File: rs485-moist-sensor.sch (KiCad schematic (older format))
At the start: 31 parts, among them IC1 ATTINY441-SSU, P1 CONN_02X03, P2 CONN_01X04, Q1 Q_PMOS_GSD, U1 SN65HVD72, U2 MCP1702, X1 16MHz

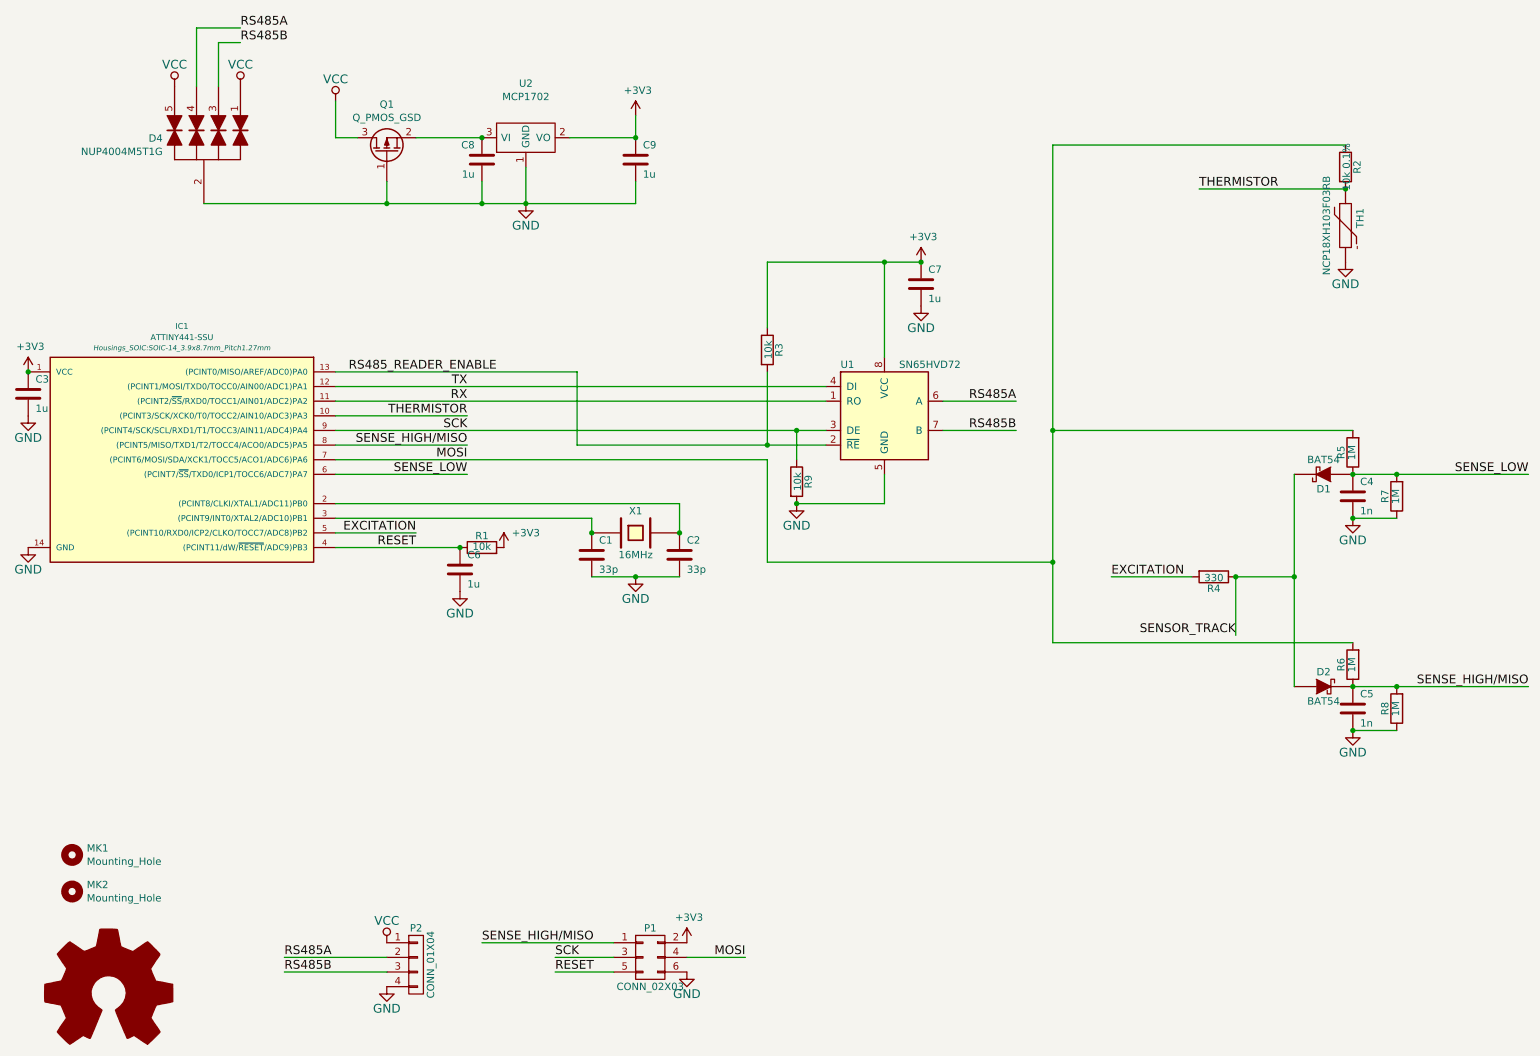
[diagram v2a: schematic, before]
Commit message: Update capacitance to accomodate crystal change. Tidyup fabrication layers
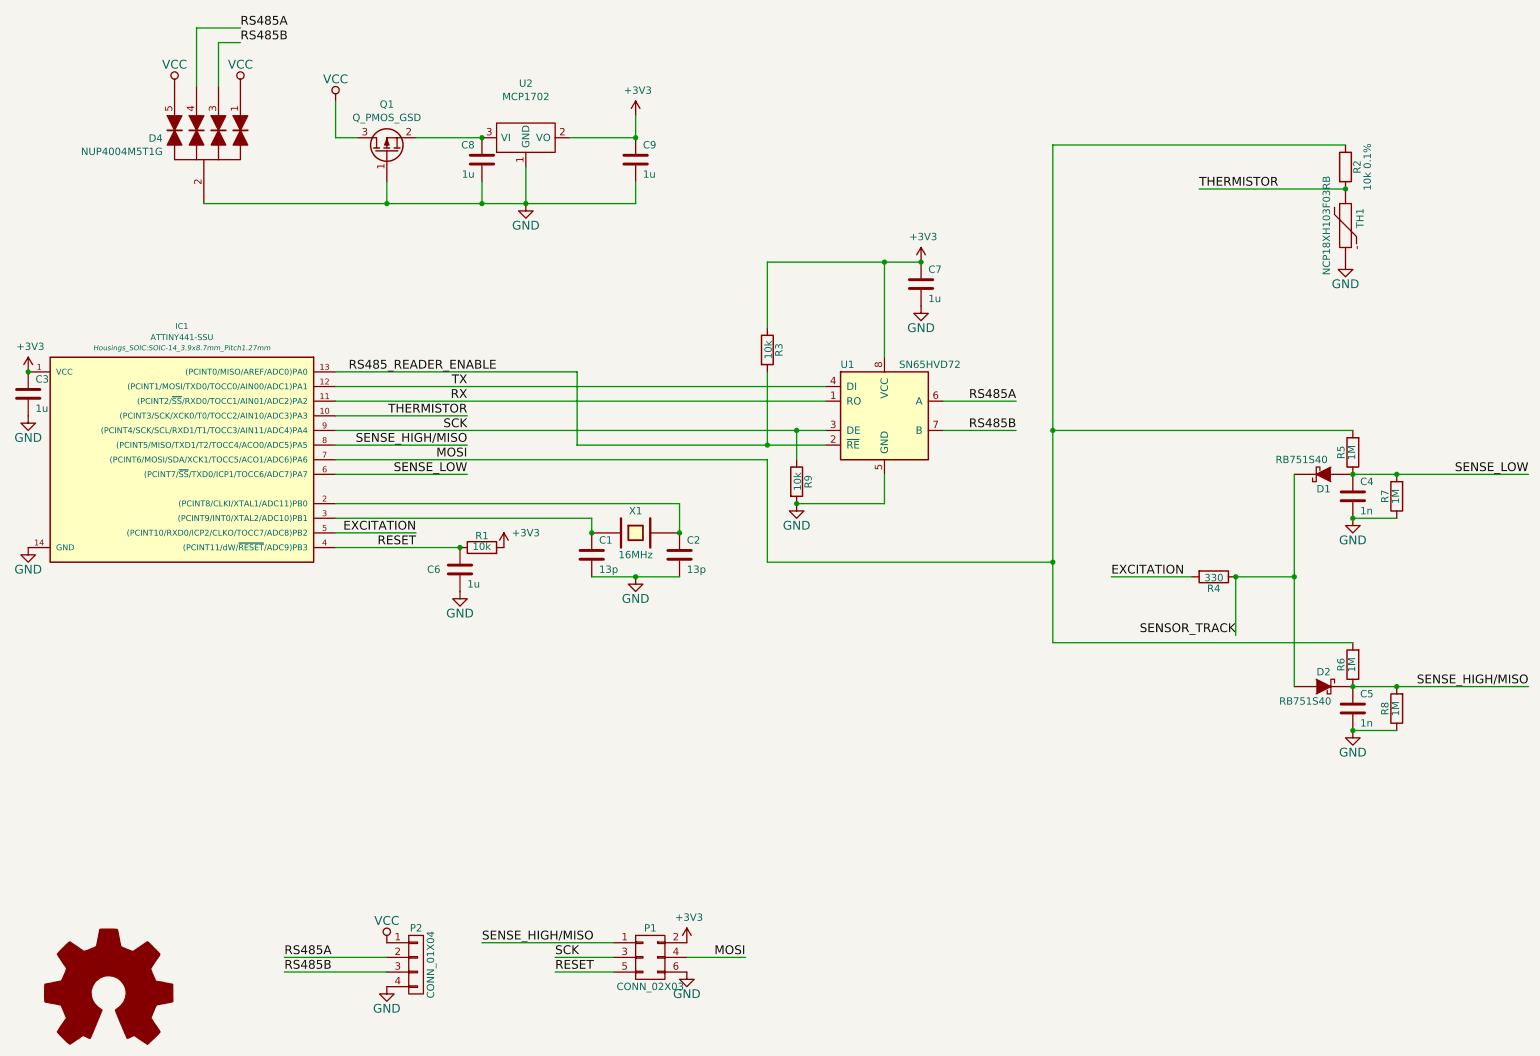
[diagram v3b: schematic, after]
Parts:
- removed MK1, MK2: Mounting_Hole, Mounting_Holes:MountingHole_3mm, symbol rs485-moist-sensor-rescue:Mounting_Hole
- C1, C2: value 33p -> 13p
- D1, D2: value BAT54 -> RB751S40
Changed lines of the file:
@@
 encoding utf-8
 Sheet 1 1
-Title "Digital soil moisture sensor"
-Date "2017-04-25"
+Title "RS485 soil moisture sensor"
+Date "2019-10-22"
 Rev ""
 Comp "Catnip electronics"
@@
 P 5150 4350
 F 0 "C2" H 5200 4450 50  0000 L CNN
-F 1 "33p" H 5200 4250 50  0000 L CNN
+F 1 "13p" H 5200 4250 50  0000 L CNN
 F 2 "Capacitors_SMD:C_0603" H 5188 4200 30  0001 C CNN
 F 3 "" H 5150 4350 60  0000 C CNN
@@
 $EndComp
 $Comp
-L power:GND #PWR13
+L power:GND #PWR013
 U 1 1 54D21A04
 P 4850 4500
-F 0 "#PWR13" H 4850 4250 60  0001 C CNN
+F 0 "#PWR013" H 4850 4250 60  0001 C CNN
 F 1 "GND" H 4850 4350 60  0000 C CNN
 F 2 "" H 4850 4500 60  0000 C CNN
@@
 $EndComp
 $Comp
-L power:VCC #PWR6
+L power:VCC #PWR06
 U 1 1 54D21DD5
 P 2800 1250
-F 0 "#PWR6" H 2800 1100 60  0001 C CNN
+F 0 "#PWR06" H 2800 1100 60  0001 C CNN
 F 1 "VCC" H 2800 1400 60  0000 C CNN
 F 2 "" H 2800 1250 60  0000 C CNN
@@
 $EndComp
 $Comp
-L power:GND #PWR3
+L power:GND #PWR03
 U 1 1 54D21DE7
 P 700 4300
-F 0 "#PWR3" H 700 4050 60  0001 C CNN
+F 0 "#PWR03" H 700 4050 60  0001 C CNN
 F 1 "GND" H 700 4150 60  0000 C CNN
 F 2 "" H 700 4300 60  0000 C CNN
@@
 $EndComp
 $Comp
-L power:GND #PWR2
+L power:GND #PWR02
 U 1 1 54D21F25
 P 700 3400
-F 0 "#PWR2" H 700 3150 60  0001 C CNN
+F 0 "#PWR02" H 700 3150 60  0001 C CNN
 F 1 "GND" H 700 3250 60  0000 C CNN
 F 2 "" H 700 3400 60  0000 C CNN
@@
 P 9550 3800
 F 0 "D1" H 9550 3900 50  0000 C CNN
-F 1 "BAT54" H 9550 3700 50  0000 C CNN
+F 1 "RB751S40" H 9700 3700 50  0000 C CNN
 F 2 "SMD_Packages:SOD-523" H 9550 3800 60  0001 C CNN
 F 3 "" H 9550 3800 60  0000 C CNN
@@
 $EndComp
 $Comp
-L power:GND #PWR21
+L power:GND #PWR021
 U 1 1 54D2221D
 P 9750 5550
-F 0 "#PWR21" H 9750 5300 60  0001 C CNN
+F 0 "#PWR021" H 9750 5300 60  0001 C CNN
 F 1 "GND" H 9750 5400 60  0000 C CNN
 F 2 "" H 9750 5550 60  0000 C CNN
@@
 $EndComp
 $Comp
-L power:GND #PWR20
+L power:GND #PWR020
 U 1 1 54D222DF
 P 9750 4100
-F 0 "#PWR20" H 9750 3850 60  0001 C CNN
+F 0 "#PWR020" H 9750 3850 60  0001 C CNN
 F 1 "GND" H 9750 3950 60  0000 C CNN
 F 2 "" H 9750 4100 60  0000 C CNN
@@
 SENSOR_TRACK
 $Comp
-L power:GND #PWR15
+L power:GND #PWR015
 U 1 1 54D22F14
 P 5200 7200
-F 0 "#PWR15" H 5200 6950 60  0001 C CNN
+F 0 "#PWR015" H 5200 6950 60  0001 C CNN
 F 1 "GND" H 5200 7050 60  0000 C CNN
 F 2 "" H 5200 7200 60  0000 C CNN
@@
 $EndComp
 $Comp
-L power:GND #PWR18
+L power:GND #PWR018
 U 1 1 54DF0CCD
 P 6800 2650
-F 0 "#PWR18" H 6800 2400 60  0001 C CNN
+F 0 "#PWR018" H 6800 2400 60  0001 C CNN
 F 1 "GND" H 6800 2500 60  0000 C CNN
 F 2 "" H 6800 2650 60  0000 C CNN
@@
 $EndComp
 $Comp
-L power:GND #PWR16
+L power:GND #PWR016
 U 1 1 54DF15E6
 P 5950 4000
-F 0 "#PWR16" H 5950 3750 60  0001 C CNN
+F 0 "#PWR016" H 5950 3750 60  0001 C CNN
 F 1 "GND" H 5950 3850 60  0000 C CNN
 F 2 "" H 5950 4000 60  0000 C CNN
@@
 U 1 1 54DF1D15
 P 3650 4450
-F 0 "C6" H 3700 4550 50  0000 L CNN
+F 0 "C6" H 3425 4450 50  0000 L CNN
 F 1 "1u" H 3700 4350 50  0000 L CNN
 F 2 "Capacitors_SMD:C_0603" H 3688 4300 30  0001 C CNN
@@
 $EndComp
 $Comp
-L power:GND #PWR9
+L power:GND #PWR09
 U 1 1 54DF1D84
 P 3650 4600
-F 0 "#PWR9" H 3650 4350 60  0001 C CNN
+F 0 "#PWR09" H 3650 4350 60  0001 C CNN
 F 1 "GND" H 3650 4450 60  0000 C CNN
 F 2 "" H 3650 4600 60  0000 C CNN
@@
 P 9700 1700
 F 0 "R2" V 9780 1700 50  0000 C CNN
-F 1 "10k 0.1%" V 9707 1701 50  0000 C CNN
+F 1 "10k 0.1%" V 9850 1700 50  0000 C CNN
 F 2 "Resistors_SMD:R_0603" V 9630 1700 30  0001 C CNN
 F 3 "" H 9700 1700 30  0000 C CNN
@@
 $EndComp
 $Comp
-L power:GND #PWR19
+L power:GND #PWR019
 U 1 1 54E0608E
 P 9700 2350
-F 0 "#PWR19" H 9700 2100 60  0001 C CNN
+F 0 "#PWR019" H 9700 2100 60  0001 C CNN
 F 1 "GND" H 9700 2200 60  0000 C CNN
 F 2 "" H 9700 2350 60  0000 C CNN
@@
 $EndComp
 $Comp
-L power:VCC #PWR7
+L power:VCC #PWR07
 U 1 1 54E1FEA9
 P 3150 7000
-F 0 "#PWR7" H 3150 6850 60  0001 C CNN
+F 0 "#PWR07" H 3150 6850 60  0001 C CNN
 F 1 "VCC" H 3150 7150 60  0000 C CNN
 F 2 "" H 3150 7000 60  0000 C CNN
@@
 $EndComp
 $Comp
-L power:GND #PWR8
+L power:GND #PWR08
 U 1 1 54E1FECE
 P 3150 7300
-F 0 "#PWR8" H 3150 7050 60  0001 C CNN
+F 0 "#PWR08" H 3150 7050 60  0001 C CNN
 F 1 "GND" H 3150 7150 60  0000 C CNN
 F 2 "" H 3150 7300 60  0000 C CNN
@@
 $EndComp
 $Comp
-L power:GND #PWR11
+L power:GND #PWR011
 U 1 1 58946682
 P 4100 1950
-F 0 "#PWR11" H 4100 1700 60  0001 C CNN
+F 0 "#PWR011" H 4100 1700 60  0001 C CNN
 F 1 "GND" H 4100 1800 60  0000 C CNN
 F 2 "" H 4100 1950 60  0000 C CNN
@@
 	4850 1950 4850 1800
 $Comp
-L power:+3V3 #PWR12
+L power:+3V3 #PWR012
 U 1 1 5894698F
 P 4850 1350
-F 0 "#PWR12" H 2050 400 50  0001 C CNN
+F 0 "#PWR012" H 2050 400 50  0001 C CNN
 F 1 "+3V3" H 4865 1523 50  0000 C CNN
 F 2 "" H 2050 550 60  0000 C CNN
@@
 	4850 1500 4850 1350
 $Comp
-L power:+3V3 #PWR1
+L power:+3V3 #PWR01
 U 1 1 58946A8E
 P 700 3100
-F 0 "#PWR1" H -2100 2150 50  0001 C CNN
+F 0 "#PWR01" H -2100 2150 50  0001 C CNN
 F 1 "+3V3" H 715 3273 50  0000 C CNN
 F 2 "" H -2100 2300 60  0000 C CNN
@@
 $EndComp
 $Comp
-L power:+3V3 #PWR17
+L power:+3V3 #PWR017
 U 1 1 58946C25
 P 6800 2350
-F 0 "#PWR17" H 4000 1400 50  0001 C CNN
+F 0 "#PWR017" H 4000 1400 50  0001 C CNN
 F 1 "+3V3" H 6815 2523 50  0000 C CNN
 F 2 "" H 4000 1550 60  0000 C CNN
@@
 Connection ~ 6800 2350
 $Comp
-L power:+3V3 #PWR14
+L power:+3V3 #PWR014
 U 1 1 589472AD
 P 5200 7000
-F 0 "#PWR14" H 2400 6050 50  0001 C CNN
+F 0 "#PWR014" H 2400 6050 50  0001 C CNN
 F 1 "+3V3" H 5215 7173 50  0000 C CNN
 F 2 "" H 2400 6200 60  0000 C CNN
@@
 $EndComp
 $Comp
-L power:+3V3 #PWR10
+L power:+3V3 #PWR010
 U 1 1 58947B36
 P 3950 4300
-F 0 "#PWR10" H 1150 3350 50  0001 C CNN
+F 0 "#PWR010" H 1150 3350 50  0001 C CNN
 F 1 "+3V3" H 4100 4400 50  0000 C CNN
 F 2 "" H 1150 3500 60  0000 C CNN
@@
 $EndComp
 $Comp
-L power:VCC #PWR4
+L power:VCC #PWR04
 U 1 1 58971B39
 P 1700 1150
-F 0 "#PWR4" H 1700 1000 60  0001 C CNN
+F 0 "#PWR04" H 1700 1000 60  0001 C CNN
 F 1 "VCC" H 1700 1300 60  0000 C CNN
 F 2 "" H 1700 1150 60  0000 C CNN
@@
 $EndComp
 $Comp
-L power:VCC #PWR5
+L power:VCC #PWR05
 U 1 1 58972379
 P 2150 1150
-F 0 "#PWR5" H 2150 1000 60  0001 C CNN
+F 0 "#PWR05" H 2150 1000 60  0001 C CNN
 F 1 "VCC" H 2150 1300 60  0000 C CNN
 F 2 "" H 2150 1150 60  0000 C CNN
@@
 P 4550 4350
 F 0 "C1" H 4600 4450 50  0000 L CNN
-F 1 "33p" H 4600 4250 50  0000 L CNN
+F 1 "13p" H 4600 4250 50  0000 L CNN
 F 2 "Capacitors_SMD:C_0603" H 4588 4200 30  0001 C CNN
 F 3 "" H 4550 4350 60  0000 C CNN
@@
 P 9550 5250
 F 0 "D2" H 9550 5350 50  0000 C CNN
-F 1 "BAT54" H 9550 5150 50  0000 C CNN
+F 1 "RB751S40" H 9425 5150 50  0000 C CNN
 F 2 "SMD_Packages:SOD-523" H 9550 5250 60  0001 C CNN
 F 3 "" H 9550 5250 60  0000 C CNN
@@
 Connection ~ 9750 5250
 $Comp
-L rs485-moist-sensor-rescue:Mounting_Hole MK1
-U 1 1 59477C0A
-P 1000 6400
-F 0 "MK1" H 1100 6446 50  0000 L CNN
-F 1 "Mounting_Hole" H 1100 6355 50  0000 L CNN
-F 2 "Mounting_Holes:MountingHole_3mm" H 1000 6400 50  0001 C CNN
-F 3 "" H 1000 6400 50  0001 C CNN
-	1    1000 6400
-	1    0    0    -1
-$EndComp
-$Comp
-L rs485-moist-sensor-rescue:Mounting_Hole MK2
-U 1 1 59477C98
-P 1000 6650
-F 0 "MK2" H 1100 6696 50  0000 L CNN
-F 1 "Mounting_Hole" H 1100 6605 50  0000 L CNN
-F 2 "Mounting_Holes:MountingHole_3mm" H 1000 6650 50  0001 C CNN
-F 3 "" H 1000 6650 50  0001 C CNN
-	1    1000 6650
-	1    0    0    -1
-$EndComp
-$Comp
 L rs485-moist-sensor-rescue:Logo_Open_Hardware_Large #LOGO1
